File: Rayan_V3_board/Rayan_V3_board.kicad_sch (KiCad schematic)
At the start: 0 parts

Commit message: Practice
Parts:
- added Becka's_Resista: R, symbol Device:R
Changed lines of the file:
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@@
 	(generator_version "9.0")
 	(paper "A4")
+	(symbol
+		(lib_id "Device:R")
+		(at 33.02 78.74 0)
+		(unit 1)
+		(exclude_from_sim no)
+		(in_bom yes)
+		(on_board yes)
+		(dnp no)
+		(fields_autoplaced yes)
+		(property "Reference" "Becka's_Resista"
+			(at 35.56 77.4699 0)
+			(effects
+				(font
+					(size 1.27 1.27)
+				)
+				(justify left)
+			)
+		)
+		(property "Value" "R"
+			(at 35.56 80.0099 0)
+			(effects
+				(font
+					(size 1.27 1.27)
+				)
+				(justify left)
+			)
+		)
+		(property "Footprint" ""
+			(at 31.242 78.74 90)
+			(effects
+				(font
+					(size 1.27 1.27)
+				)
+				(hide yes)
+			)
+		)
+		(property "Datasheet" "~"
+			(at 33.02 78.74 0)
+			(effects
+				(font
+					(size 1.27 1.27)
+				)
+				(hide yes)
+			)
+		)
+		(property "Description" "Resistor"
+			(at 33.02 78.74 0)
+			(effects
+				(font
+					(size 1.27 1.27)
+				)
+				(hide yes)
+			)
+		)
+		(pin "1"
+		)
+		(pin "2"
+		)
+		(instances
+			(project ""
+				(path "/85cd2bc3-b142-4c9a-a9f2-621b4ed83fca"
+					(reference "Becka's_Resista")
+					(unit 1)
+				)
+			)
+		)
+	)
 	(sheet
 		(at 25.4 20.32)

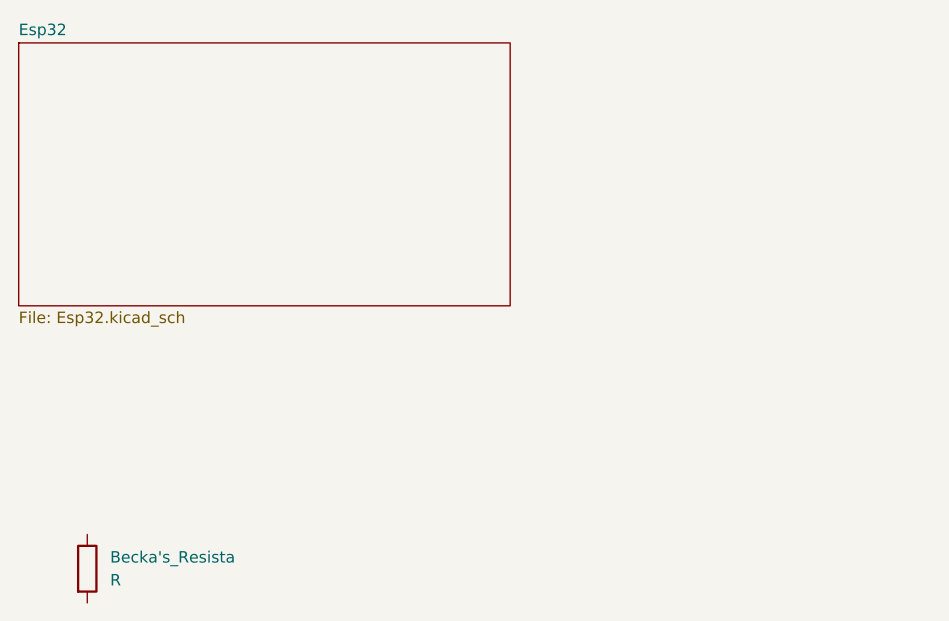
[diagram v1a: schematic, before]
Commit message: Added Motor Controllers
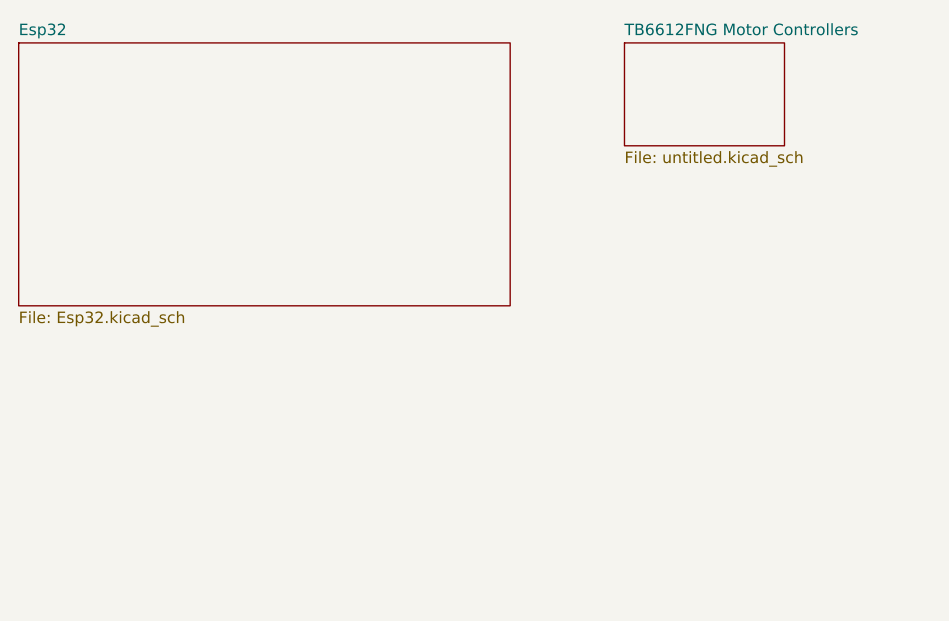
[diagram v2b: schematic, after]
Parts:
- removed Becka's_Resista: R, symbol Device:R
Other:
- added sheet TB6612FNG Motor Controllers (untitled.kicad_sch)
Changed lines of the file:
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@@
 	(generator_version "9.0")
 	(paper "A4")
-	(symbol
-		(lib_id "Device:R")
-		(at 33.02 78.74 0)
-		(unit 1)
-		(exclude_from_sim no)
-		(in_bom yes)
-		(on_board yes)
-		(dnp no)
-		(fields_autoplaced yes)
-		(property "Reference" "Becka's_Resista"
-			(at 35.56 77.4699 0)
-			(effects
-				(font
-					(size 1.27 1.27)
-				)
-				(justify left)
-			)
-		)
-		(property "Value" "R"
-			(at 35.56 80.0099 0)
-			(effects
-				(font
-					(size 1.27 1.27)
-				)
-				(justify left)
-			)
-		)
-		(property "Footprint" ""
-			(at 31.242 78.74 90)
-			(effects
-				(font
-					(size 1.27 1.27)
-				)
-				(hide yes)
-			)
-		)
-		(property "Datasheet" "~"
-			(at 33.02 78.74 0)
-			(effects
-				(font
-					(size 1.27 1.27)
-				)
-				(hide yes)
-			)
-		)
-		(property "Description" "Resistor"
-			(at 33.02 78.74 0)
-			(effects
-				(font
-					(size 1.27 1.27)
-				)
-				(hide yes)
-			)
-		)
-		(pin "1"
-		)
-		(pin "2"
-		)
-		(instances
-			(project ""
-				(path "/85cd2bc3-b142-4c9a-a9f2-621b4ed83fca"
-					(reference "Becka's_Resista")
-					(unit 1)
-				)
-			)
-		)
-	)
 	(sheet
 		(at 25.4 20.32)
@@
 				)
 			)
+		)
+	)
+	(sheet
+		(at 92.71 20.32)
+		(size 17.78 11.43)
+		(exclude_from_sim no)
+		(in_bom yes)
+		(on_board yes)
+		(dnp no)
+		(fields_autoplaced yes)
+		(stroke
+			(width 0.1524)
+			(type solid)
+		)
+		(fill
+			(color 0 0 0 0.0000)
+		)
+		(property "Sheetname" "TB6612FNG Motor Controllers"
+			(at 92.71 19.6084 0)
+			(effects
+				(font
+					(size 1.27 1.27)
+				)
+				(justify left bottom)
+			)
+		)
+		(property "Sheetfile" "untitled.kicad_sch"
+			(at 92.71 32.3346 0)
+			(effects
+				(font
+					(size 1.27 1.27)
+				)
+				(justify left top)
+			)
+		)
+		(instances
+			(project "Rayan_V3_board"
+				(path "/85cd2bc3-b142-4c9a-a9f2-621b4ed83fca"
+					(page "3")
+				)
+			)
